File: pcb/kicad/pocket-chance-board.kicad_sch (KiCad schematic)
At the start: 144 parts, among them J1 SWD, J2 USB4085-GF-A, J3 LiPo JST-PH 2.0mm (1 = + RED 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, J4 LCD 1.54in ST7789 module, JST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, J5 Speaker JST-PH, J6 microSD Molex 104031-0811, J7 STEMMA QT, J8 Expansion (6 = VBAT_SENSE ADC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, J9 LCD header 2.54 mm (wire by n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, Q1 FS8205A, Q3 AO3400A, Q4 AO3401A, Q6 AO3401A (DNP: fit only for a 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, SW1 BOOT, SW10 DPAD LEFT PTS645SM43SMTR92, SW11 DPAD RIGHT PTS645SM43SMTR92, SW12 DPAD PRESS PTS645SM43SMTR92, SW2 RESET, SW3 POWER PCM12, SW4 A PTS125SM43SMTR2LFS, SW5 B PTS125SM43SMTR2LFS, SW6 X PTS125SM43SMTR2LFS, SW7 Y PTS125SM43SMTR2LFS, SW8 DPAD UP PTS645SM43SMTR92, SW9 DPAD DOWN PTS645SM43SMTR92, U1 RP2350A, U10 LSM6DSOXTR, U11 RM2, U2 W25Q128JVSIQ, U3 APS6404L-3SQR-SN, U4 USBLC6-2SC6, U5 BQ24074RGTR, U6 TPS63001DRCR, U7 DW01A, U8 PAM8302AADCR, U9 DS3231MZ+, Y1 12MHz ABM8-272-T3

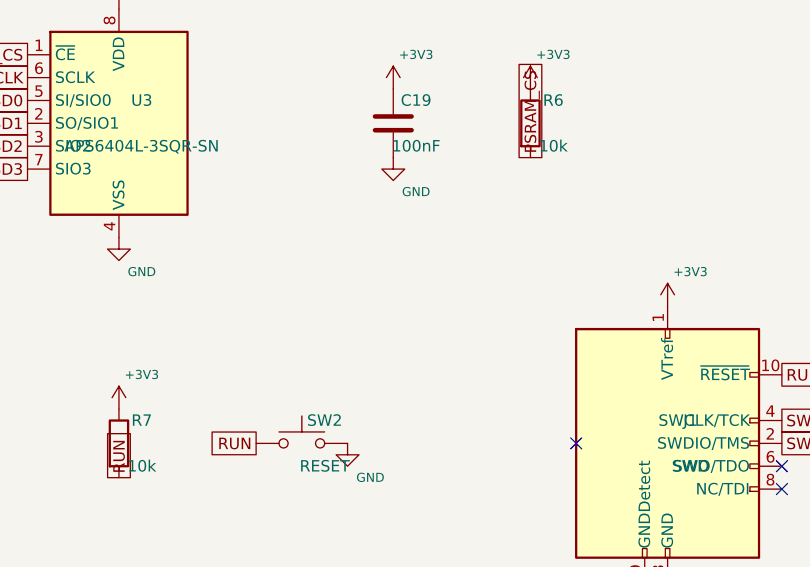
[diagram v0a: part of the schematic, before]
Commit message: Rev 0.13 (John's yes): C44 1 uF 0603 at PSRAM VDD pin 8 (APS6404L-3SQR section 14.3); J-SD row corrected to push-pull
Netlist diff vs rev 0.12 (8e8ce9e): C44 added on +3V3/GND, nothing else. ERC 0 errors, 2 expected
warnings. Placed at (93.5, 56.6) beside U3 pin 8; DRC only unrouted connections.

Co-Authored-By: Claude Opus 5.5 <noreply@anthropic.com>
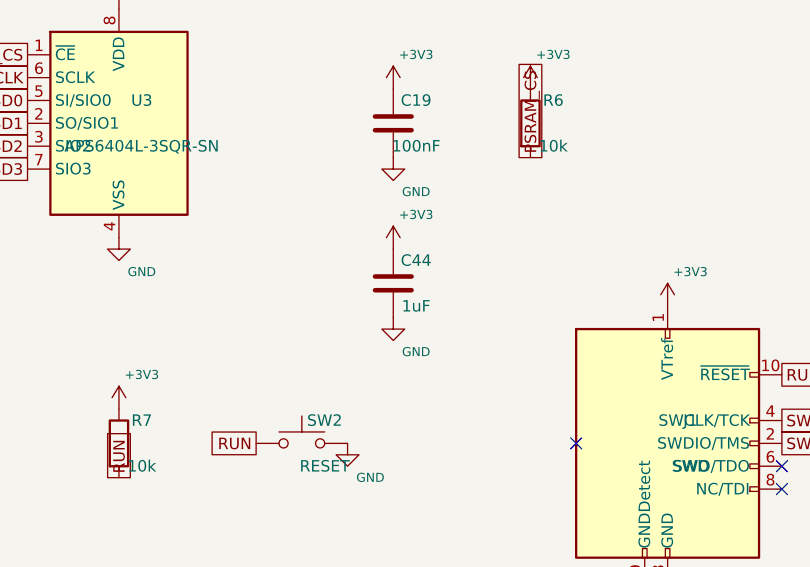
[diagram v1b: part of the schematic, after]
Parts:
- added C44: 1uF, Capacitor_SMD:C_0603_1608Metric, symbol Device:C
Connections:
- net +3V3: now also C44.1
- net GND: now also C44.2
